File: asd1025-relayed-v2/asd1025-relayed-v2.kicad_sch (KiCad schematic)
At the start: 20 parts, among them J1 DF3-12S-2DSA, J2 DF3-12S-2DSA, J3 DF3-12S-2DSA, J4 Conn_01x04_Male, J5 Conn_01x01_Female, J6 Conn_01x01_Female, K1 EC2-5NU, K2 EC2-5NU, K3 EC2-5NU, K4 EC2-5NU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

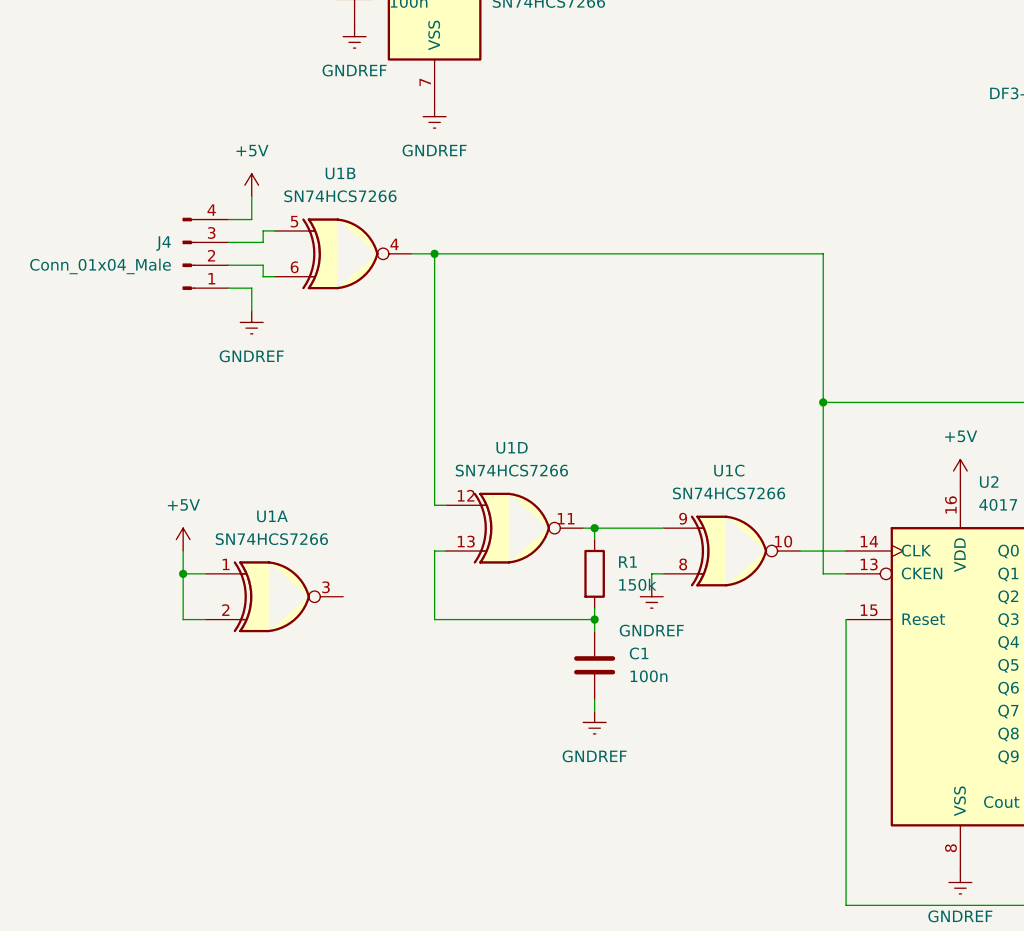
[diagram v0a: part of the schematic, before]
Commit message: fix mistake in v2 board about oscillator timing logic, nicer bottom silkscreen, no clock enabled signal needed anymore
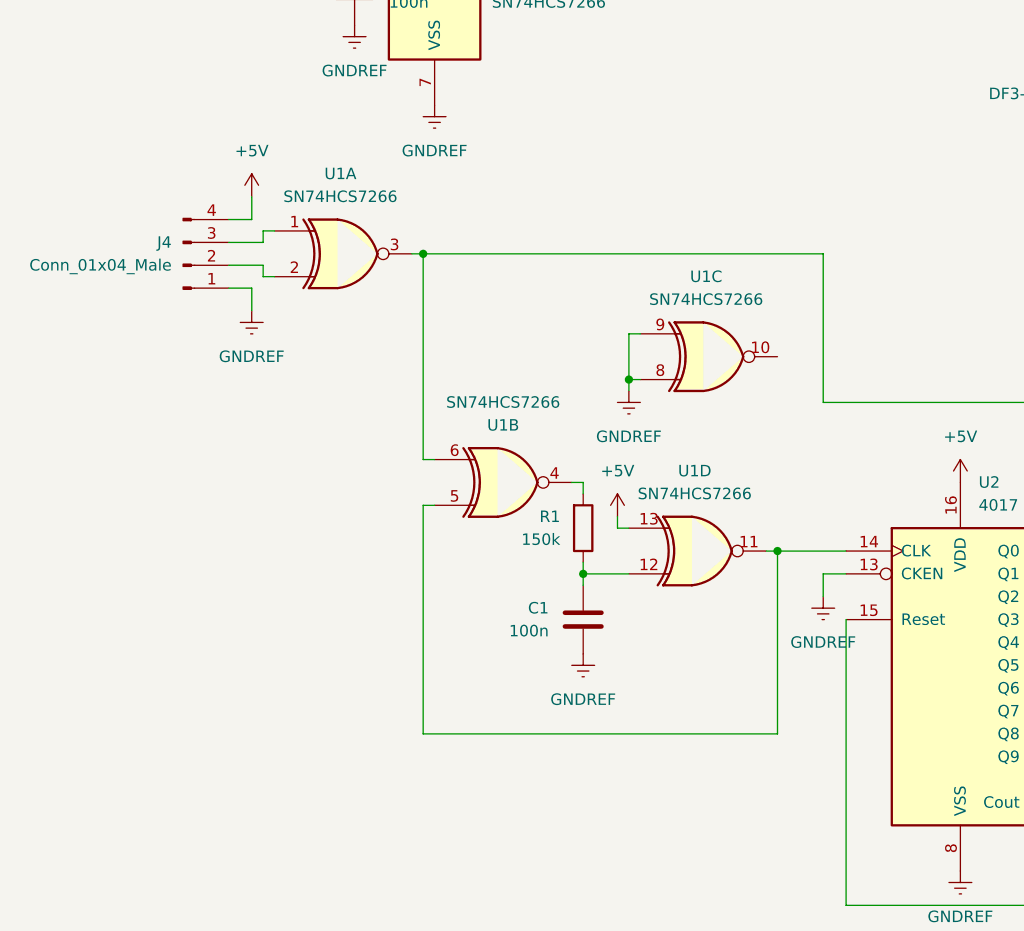
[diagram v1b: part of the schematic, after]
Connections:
- net +5V: now also U1.13; no longer U1.1, U1.2
- net GNDREF: now also C1.1, U1.9, U2.13 (CKEN); no longer C1.2
- net at U1.10: no longer U2.14 (CLK)
- net at U1.3: now also Q1.1 (B), U1.6
- net at U1.5: now also U1.11, U2.14 (CLK); no longer J4.3 (Pin_3)
- net at J4.2 (Pin_2): now also U1.2; no longer U1.6
- new net: C1.2, R1.1, U1.12
- new net: R1.2, U1.4
- new net: J4.3 (Pin_3), U1.1
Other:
- moved on the sheet: C1, R1, U1A, U1B, U1C, U1D

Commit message: change oscillator frequency to minimum to ensure 10ms between relai cut-off and on-switching
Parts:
- R1: value 150k -> 120k
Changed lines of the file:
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@@
       (effects (font (size 1.27 1.27)) (justify right))
     )
-    (property "Value" "150k" (id 1) (at 74.93 97.7899 0)
+    (property "Value" "120k" (id 1) (at 74.93 97.7899 0)
       (effects (font (size 1.27 1.27)) (justify right))
     )
@@
     )
     (path "/22ce056b-1b36-4367-abfd-97ef53b41380"
-      (reference "R1") (unit 1) (value "150k") (footprint "Resistor_THT:R_Axial_DIN0207_L6.3mm_D2.5mm_P10.16mm_Horizontal")
+      (reference "R1") (unit 1) (value "120k") (footprint "Resistor_THT:R_Axial_DIN0207_L6.3mm_D2.5mm_P10.16mm_Horizontal")
     )
     (path "/56fb3485-dc73-4e1b-824c-604483007889"

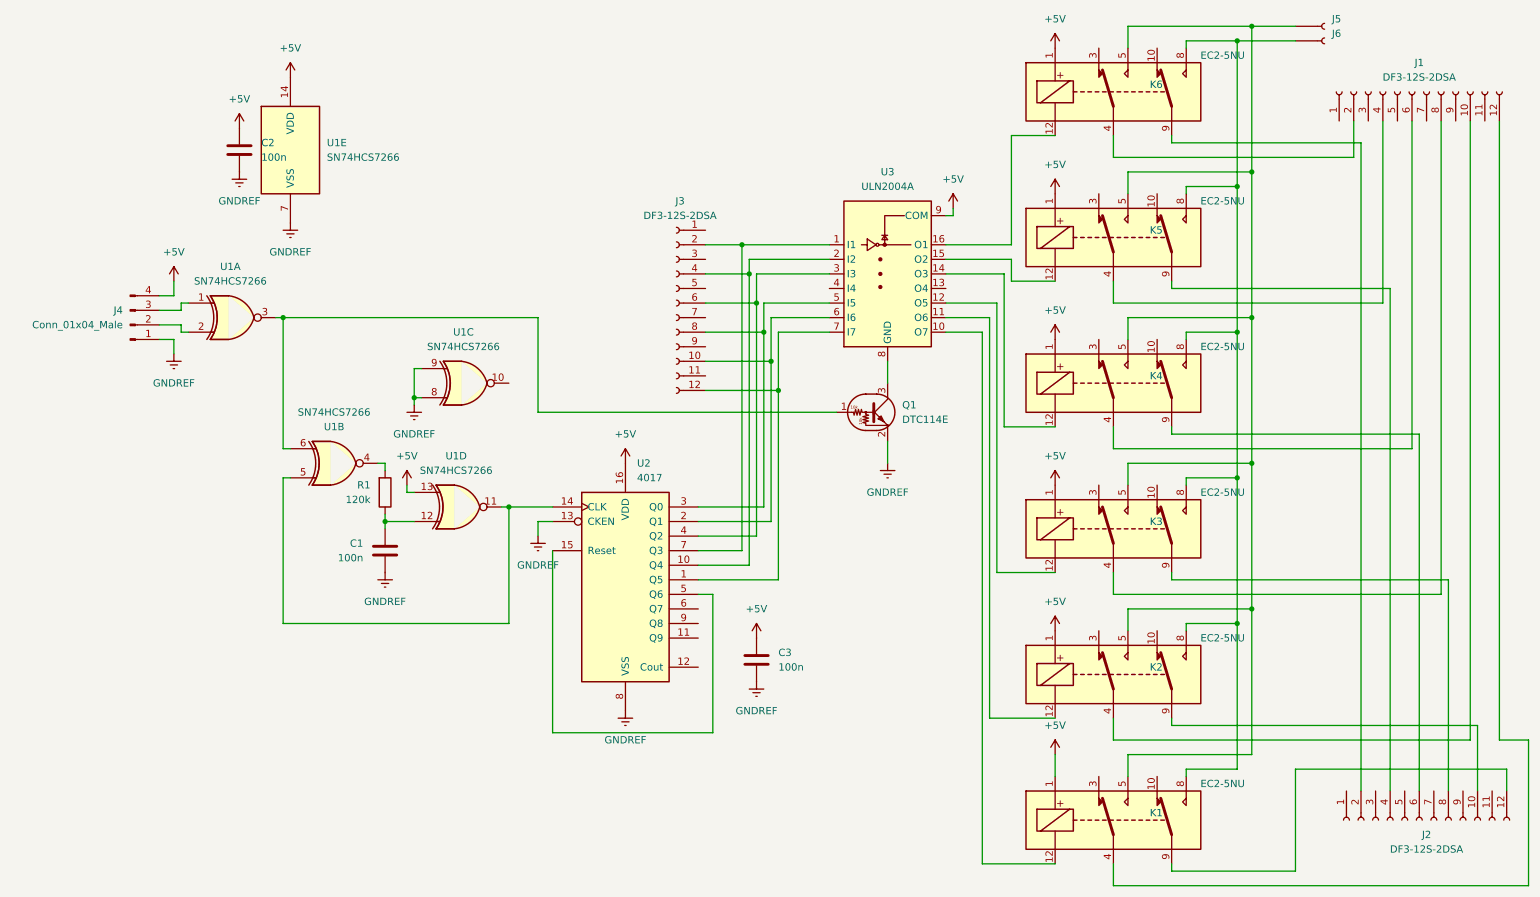
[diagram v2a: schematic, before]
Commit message: fix v2: relays would switch by passing current through base-emittor-resistors in darlington array even if main transistor Q1 is off
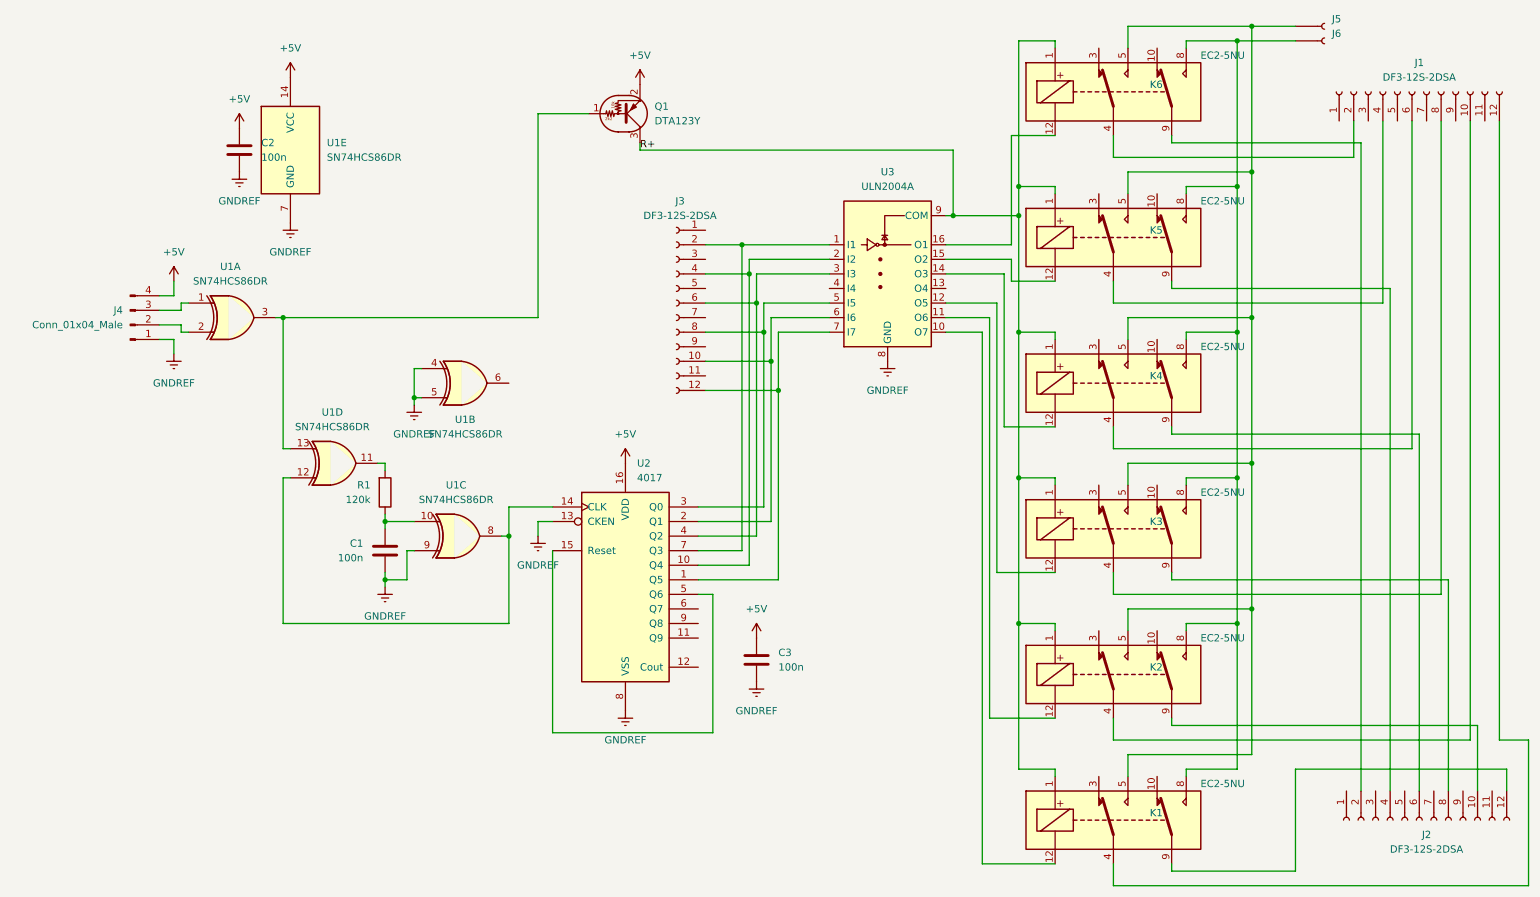
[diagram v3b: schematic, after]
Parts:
- removed Q1: DTC114E, Package_TO_SOT_SMD:SOT-23, symbol Transistor_BJT:DTC114E
- added Q1: DTA123Y, Package_TO_SOT_SMD:SOT-23, symbol Transistor_BJT:DTA123Y
- U1: value SN74HCS7266 -> SN74HCS86DR; symbol 4xxx:4077 -> 74xx:74HC86
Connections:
- net +5V: now also Q1.2 (E); no longer K1.1, K2.1, K3.1, K4.1, K5.1, K6.1, U1.13, U3.9 (COM)
- net GNDREF: now also U1.4, U1.5, U3.8 (GND); no longer U1.8
- net at U1.10: now also C1.2, R1.1
- net at R1.2: now also U1.11; no longer U1.4
- net at U1.3: now also U1.13, Q1.1 (B); no longer U1.6
- new net: U1.12, U1.8, U2.14 (CLK)
- new net R+: K1.1, K2.1, K3.1, K4.1, K5.1, K6.1, Q1.3 (C), U3.9 (COM)
